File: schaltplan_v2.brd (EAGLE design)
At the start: 100 x 80 mm, 18 parts

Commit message: layout/board redesign
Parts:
- removed D10, D3, D4, D5, D6, D7, D8, D9: 1N4004, diode:DO41-10
- removed U$3, U$4, U$5: JS_05_MN_KT, n39:JS_05_MN_KT
- removed U$6, U$7, U$8: JS_05_N_K, n39:JS_05_N_K
- added T1, T2: 2N3565, transistor:TO92
- added X1: SSW-102-02-S-S-RA, con-samtec:SSW-102-02-S-S-RA
- added X3: SSW-103-02-S-S-RA, con-samtec:SSW-103-02-S-S-RA
- added X4: SSW-109-02-S-S-RA, con-samtec:SSW-109-02-S-S-RA
- U$1: value JS_05_N_K -> JS_05_MN_KT; device n39:JS_05_N_K -> n39:JS_05_MN_KT
- U$2: value JS_05_MN_KT -> JS_05_N_K; device n39:JS_05_MN_KT -> n39:JS_05_N_K
- moved D2 122.3 mm to (6.35, -40.6), turned to 0 degrees
- moved D1 91.1 mm to (6.35, -3.81), turned to 0 degrees
- moved U$2 65.0 mm to (1.27, -29.2), turned to 0 degrees
- moved U$1 58.5 mm to (1.27, -17.8), turned to 0 degrees
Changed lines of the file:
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@@
 </autorouter>
 <elements>
-<element name="D1" library="diode" package="DO41-10" value="1N4004" x="85.09" y="41.91" rot="R90"/>
-<element name="D2" library="diode" package="DO41-10" value="1N4004" x="96.52" y="41.91" rot="R90"/>
-<element name="U$1" library="n39" package="JS_05_N_K" value="JS_05_N_K" x="27.94" y="34.29" rot="R270"/>
-<element name="U$2" library="n39" package="JS_05_MN_KT" value="JS_05_MN_KT" x="15.24" y="34.29" rot="R270"/>
-<element name="U$3" library="n39" package="JS_05_MN_KT" value="JS_05_MN_KT" x="87.63" y="34.29" rot="R270"/>
-<element name="U$4" library="n39" package="JS_05_MN_KT" value="JS_05_MN_KT" x="63.5" y="34.29" rot="R270"/>
-<element name="U$5" library="n39" package="JS_05_MN_KT" value="JS_05_MN_KT" x="39.37" y="34.29" rot="R270"/>
-<element name="U$6" library="n39" package="JS_05_N_K" value="JS_05_N_K" x="3.81" y="34.29" rot="R270"/>
-<element name="U$7" library="n39" package="JS_05_N_K" value="JS_05_N_K" x="52.07" y="34.29" rot="R270"/>
-<element name="U$8" library="n39" package="JS_05_N_K" value="JS_05_N_K" x="76.2" y="34.29" rot="R270"/>
-<element name="D3" library="diode" package="DO41-10" value="1N4004" x="72.39" y="41.91" rot="R90"/>
-<element name="D4" library="diode" package="DO41-10" value="1N4004" x="60.96" y="41.91" rot="R90"/>
-<element name="D5" library="diode" package="DO41-10" value="1N4004" x="48.26" y="41.91" rot="R90"/>
-<element name="D6" library="diode" package="DO41-10" value="1N4004" x="36.83" y="41.91" rot="R90"/>
-<element name="D7" library="diode" package="DO41-10" value="1N4004" x="24.13" y="41.91" rot="R90"/>
-<element name="D8" library="diode" package="DO41-10" value="1N4004" x="12.7" y="41.91" rot="R90"/>
-<element name="D9" library="diode" package="DO41-10" value="1N4004" x="46.99" y="74.93"/>
-<element name="D10" library="diode" package="DO41-10" value="1N4004" x="59.69" y="74.93"/>
+<element name="D1" library="diode" package="DO41-10" value="1N4004" x="6.35" y="-3.81"/>
+<element name="U$1" library="n39" package="JS_05_MN_KT" value="JS_05_MN_KT" x="1.27" y="-17.78"/>
+<element name="U$2" library="n39" package="JS_05_N_K" value="JS_05_N_K" x="1.27" y="-29.21"/>
+<element name="T1" library="transistor" package="TO92" value="2N3565" x="3.81" y="-34.29"/>
+<element name="D2" library="diode" package="DO41-10" value="1N4004" x="6.35" y="-40.64"/>
+<element name="T2" library="transistor" package="TO92" value="2N3565" x="3.81" y="-46.99"/>
+<element name="X1" library="con-samtec" package="SSW-102-02-S-S-RA" value="SSW-102-02-S-S-RA" x="-5.08" y="-39.37">
+<attribute name="OC_NEWARK" value="11P9352" x="-5.08" y="-39.37" size="1.778" layer="27" display="off"/>
+<attribute name="MPN" value="SSW-102-02-S-S-RA" x="-5.08" y="-39.37" size="1.778" layer="27" display="off"/>
+<attribute name="MF" value="" x="-5.08" y="-39.37" size="1.778" layer="27" display="off"/>
+<attribute name="OC_FARNELL" value="unknown" x="-5.08" y="-39.37" size="1.778" layer="27" display="off"/>
+</element>
+<element name="X3" library="con-samtec" package="SSW-103-02-S-S-RA" value="SSW-103-02-S-S-RA" x="-3.81" y="-63.5">
+<attribute name="OC_NEWARK" value="11P9368" x="-3.81" y="-63.5" size="1.778" layer="27" display="off"/>
+<attribute name="MPN" value="SSW-103-02-S-S-RA" x="-3.81" y="-63.5" size="1.778" layer="27" display="off"/>
+<attribute name="MF" value="" x="-3.81" y="-63.5" size="1.778" layer="27" display="off"/>
+<attribute name="OC_FARNELL" value="unknown" x="-3.81" y="-63.5" size="1.778" layer="27" display="off"/>
+</element>
+<element name="X4" library="con-samtec" package="SSW-109-02-S-S-RA" value="SSW-109-02-S-S-RA" x="3.81" y="-74.93">
+<attribute name="OC_NEWARK" value="11P9466" x="3.81" y="-74.93" size="1.778" layer="27" display="off"/>
+<attribute name="MPN" value="SSW-109-02-S-S-RA" x="3.81" y="-74.93" size="1.778" layer="27" display="off"/>
+<attribute name="MF" value="" x="3.81" y="-74.93" size="1.778" layer="27" display="off"/>
+<attribute name="OC_FARNELL" value="unknown" x="3.81" y="-74.93" size="1.778" layer="27" display="off"/>
+</element>
 </elements>
 <signals>

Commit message: schaltplan_v2 finalized
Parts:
- added C1: (no value), rcl:E3,5-8
- added C2: (no value), rcl:C025-030X050
- added D10, D3, D4, D5, D6, D7, D8, D9: 1N4004, diode:DO41-10
- added R1, R2, R3, R4, R5, R6, R7, R8: (no value), resistor:0204V
- added T3, T4, T5, T6, T7, T8: 2N3565, transistor:TO92
- added U$3, U$5, U$7: JS_05_MN_KT, n39:JS_05_MN_KT
- added U$4, U$6, U$8: JS_05_N_K, n39:JS_05_N_K
- added X2: SSW-102-02-S-S-RA, con-samtec:SSW-102-02-S-S-RA
- added X5, X6, X7: SSW-103-02-S-S-RA, con-samtec:SSW-103-02-S-S-RA
- moved X4 156.2 mm to (38.1, 77.5), turned to 180 degrees
- moved X1 149.9 mm to (88.9, 77.5), turned to 180 degrees
- moved T2 118.9 mm to (74.9, 48.3)
- moved T1 115.8 mm to (85.1, 48.3)
- moved D2 108.8 mm to (78.7, 40.6), turned to 90 degrees
- moved X3 101.8 mm to (73.7, 2.54)
- moved U$1 94.4 mm to (80.0, 34.3), turned to 270 degrees
- moved D1 93.8 mm to (88.9, 40.6), turned to 90 degrees
- moved U$2 93.5 mm to (69.8, 34.3), turned to 270 degrees
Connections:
- new net N$1: X2.1, X3.1, X5.1, X6.1, X7.1
- new net N$10: C1.-, C2.2, D10.A, T1.1, T2.1, T3.1, T4.1, T5.1, T6.1, T7.1, T8.1, X4.1
- new net N$11: R2.1, X4.3
- new net N$12: D2.A, T2.3, U$2.P$1
- new net N$13: R6.2, T6.2
- new net N$14: R3.1, X4.4
- new net N$16: U$4.P$5, X5.2
- new net N$17: U$4.P$4, X5.3
- new net N$18: U$3.P$4, U$4.P$3
- new net N$2: U$2.P$5, X3.2
- new net N$20: D3.A, T3.3, U$3.P$1
- new net N$21: C1.+, C2.1, D1.C, D2.C, D3.C, D4.C, D5.C, D6.C, D7.C, D8.C, D9.C, U$1.P$2, U$2.P$2, U$3.P$2, U$4.P$2, U$5.P$2, U$6.P$2, U$7.P$2, U$8.P$2
- new net N$22: R3.2, T3.2
- new net N$23: R4.1, X4.5
- new net N$25: D4.A, T4.3, U$4.P$1
- new net N$26: R5.1, X4.6
- new net N$27: R2.2, T2.2
- new net N$28: R4.2, T4.2
- new net N$3: U$2.P$4, X3.3
- new net N$30: U$6.P$5, X6.2
- new net N$31: U$6.P$4, X6.3
- new net N$32: U$5.P$4, U$6.P$3
- new net N$34: D5.A, T5.3, U$5.P$1
- new net N$36: R5.2, T5.2
- new net N$37: R6.1, X4.7
- new net N$39: D6.A, T6.3, U$6.P$1
- new net N$4: U$1.P$4, U$2.P$3
- new net N$40: R8.2, T8.2
- new net N$42: U$8.P$5, X7.2
- new net N$43: U$8.P$4, X7.3
- new net N$44: U$7.P$4, U$8.P$3
- new net N$46: D7.A, T7.3, U$7.P$1
- new net N$48: R7.2, T7.2
- new net N$49: R7.1, X4.8
- new net N$5: U$1.P$3, U$3.P$3, U$5.P$3, U$7.P$3, X2.2
- new net N$51: D8.A, T8.3, U$8.P$1
- new net N$53: D9.A, X1.1
- new net N$54: D10.C, X1.2
- new net N$6: D1.A, T1.3, U$1.P$1
- new net N$7: R8.1, X4.9
- new net N$8: R1.2, T1.2
- new net N$9: R1.1, X4.2
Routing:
- net N$21: track 0.00 -> 262.6 mm
- net N$10: track 0.00 -> 246.6 mm
- net N$1: track 0.00 -> 110.0 mm
- net N$5: track 0.00 -> 108.6 mm
- net N$9: track 0.00 -> 59.4 mm
- net N$11: track 0.00 -> 51.8 mm
- net N$14: track 0.00 -> 42.9 mm
- net N$7: track 0.00 -> 37.8 mm
- net N$23: track 0.00 -> 35.3 mm
- net N$49: track 0.00 -> 30.2 mm
- net N$20: track 0.00 -> 28.9 mm
- net N$34: track 0.00 -> 28.8 mm
- net N$12: track 0.00 -> 28.8 mm
- net N$26: track 0.00 -> 26.4 mm
- net N$6: track 0.00 -> 23.8 mm
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
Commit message: more fixes
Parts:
- turned C1 to 270 degrees
- turned D10 to 0 degrees
- turned D9 to 180 degrees
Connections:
- removed net N$10: C1.-, C2.2, D10.A, T1.1, T2.1, T3.1, T4.1, T5.1, T6.1, T7.1, T8.1, X4.1
- removed net N$21: C1.+, C2.1, D1.C, D2.C, D3.C, D4.C, D5.C, D6.C, D7.C, D8.C, D9.C, U$1.P$2, U$2.P$2, U$3.P$2, U$4.P$2, U$5.P$2, U$6.P$2, U$7.P$2, U$8.P$2
- removed net N$53: D9.A, X1.1
- removed net N$54: D10.C, X1.2
- new net N$15: D9.C, X1.1
- new net N$19: D10.A, X1.2
- new net N$24: C1.+, C2.2, D10.C, T1.1, T2.1, T3.1, T4.1, T5.1, T6.1, T7.1, T8.1, X4.1
- new net N$29: C1.-, C2.1, D1.C, D2.C, D3.C, D4.C, D5.C, D6.C, D7.C, D8.C, D9.A, U$1.P$2, U$2.P$2, U$3.P$2, U$4.P$2, U$5.P$2, U$6.P$2, U$7.P$2, U$8.P$2
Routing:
- net N$29: track 0.00 -> 274.8 mm
- net N$21: track 262.6 -> 0.00 mm
- net N$10: track 246.6 -> 0.00 mm
- net N$24: track 0.00 -> 208.0 mm
- net N$53: track 15.0 -> 0.00 mm
- net N$15: track 0.00 -> 15.0 mm
- net N$54: track 8.64 -> 0.00 mm
- net N$19: track 0.00 -> 8.64 mm

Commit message: more fixes
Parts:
- removed X4: SSW-109-02-S-S-RA, con-samtec:SSW-109-02-S-S-RA
- added X8: SSW-110-02-S-S-RA, con-samtec:SSW-110-02-S-S-RA
- moved R1 1.27 mm to (85.1, 55.9)
- moved R2 1.27 mm to (74.9, 55.9)
- moved R3 1.27 mm to (63.5, 55.9)
- moved R4 1.27 mm to (53.3, 55.9)
- moved R5 1.27 mm to (41.9, 55.9)
- moved R6 1.27 mm to (31.8, 55.9)
- moved R7 1.27 mm to (20.3, 55.9)
- moved R8 1.27 mm to (10.2, 55.9)
- moved T1 1.27 mm to (85.1, 49.5)
- moved T2 1.27 mm to (74.9, 49.5)
- moved T3 1.27 mm to (63.5, 49.5)
- moved T4 1.27 mm to (53.3, 49.5)
- moved T5 1.27 mm to (41.9, 49.5)
- moved T6 1.27 mm to (31.8, 49.5)
- moved T7 1.27 mm to (20.3, 49.5)
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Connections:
- removed net N$29 (its old number): C1.-, C2.1, D1.C, D2.C, D3.C, D4.C, D5.C, D6.C, D7.C, D8.C, D9.A, U$1.P$2, U$2.P$2, U$3.P$2, U$4.P$2, U$5.P$2, U$6.P$2, U$7.P$2, U$8.P$2
- new net N$19: C1.-, C2.1, D9.A, T1.1, T2.1, T3.1, T4.1, T5.1, T6.1, T7.1, T8.1, X8.10
- net N$11: now also X8.3; no longer X4.3
- net N$14: now also X8.4; no longer X4.4
- net N$23: now also X8.5; no longer X4.5
- net N$24: now also D1.C, D2.C, D3.C, D4.C, D5.C, D6.C, D7.C, D8.C, U$1.P$2, U$2.P$2, U$3.P$2, U$4.P$2, U$5.P$2, U$6.P$2, U$7.P$2, U$8.P$2, X8.1; no longer T1.1, T2.1, T3.1, T4.1, T5.1, T6.1, T7.1, T8.1, X4.1
- net N$26: now also X8.6; no longer X4.6
- net N$37: now also X8.7; no longer X4.7
- net N$49: now also X8.8; no longer X4.8
- net N$7: now also X8.9; no longer X4.9
- net N$9: now also X8.2; no longer X4.2
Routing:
- net N$29 (its old number): track 274.8 -> 0.00 mm
- net N$19: track 0.00 -> 224.3 mm
- net N$24: track 208.0 -> 270.6 mm
- net N$7: track 37.8 -> 59.4 mm
- net N$49: track 30.2 -> 42.9 mm
- net N$9: track 59.4 -> 56.9 mm
- net N$11: track 51.8 -> 49.3 mm
- net N$26: track 26.4 -> 23.9 mm
- net N$23: track 35.3 -> 32.8 mm
- net N$14: track 42.9 -> 40.4 mm

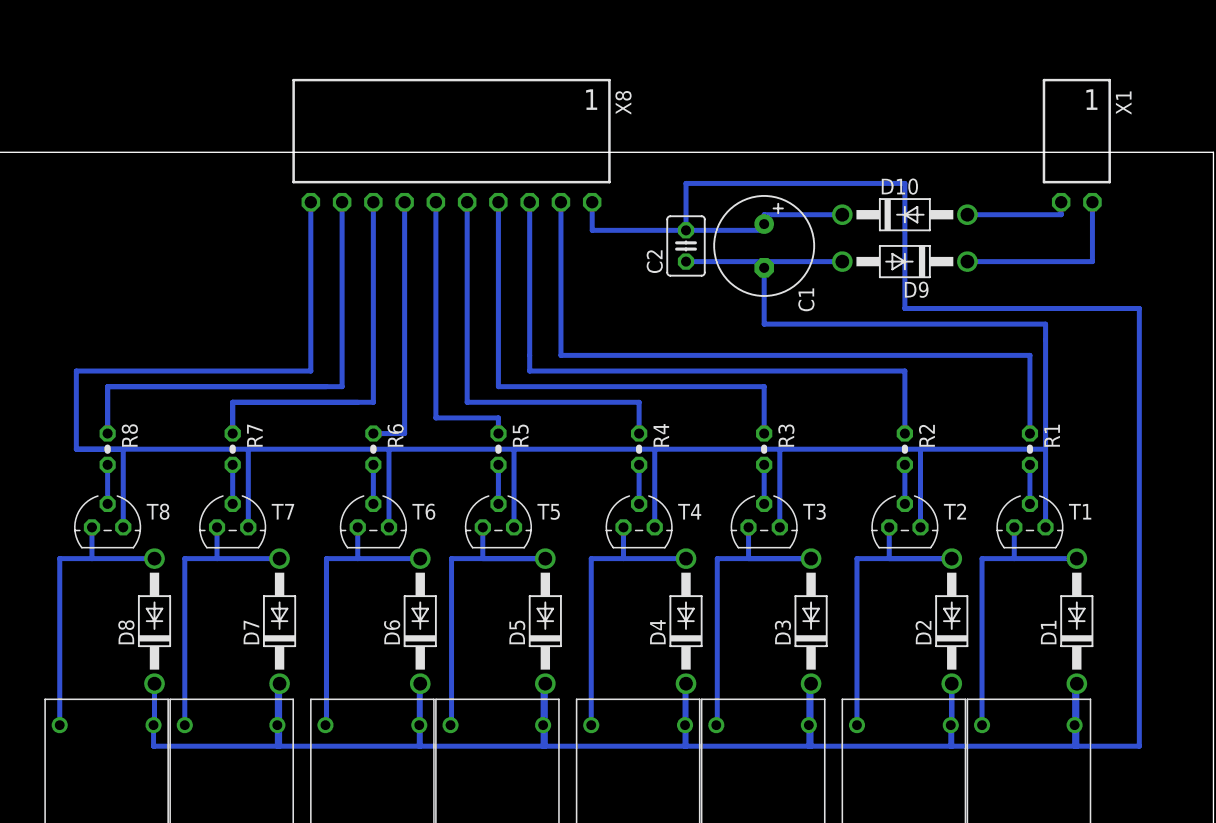
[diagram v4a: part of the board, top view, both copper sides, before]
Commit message: change 9pin connector to sub-d
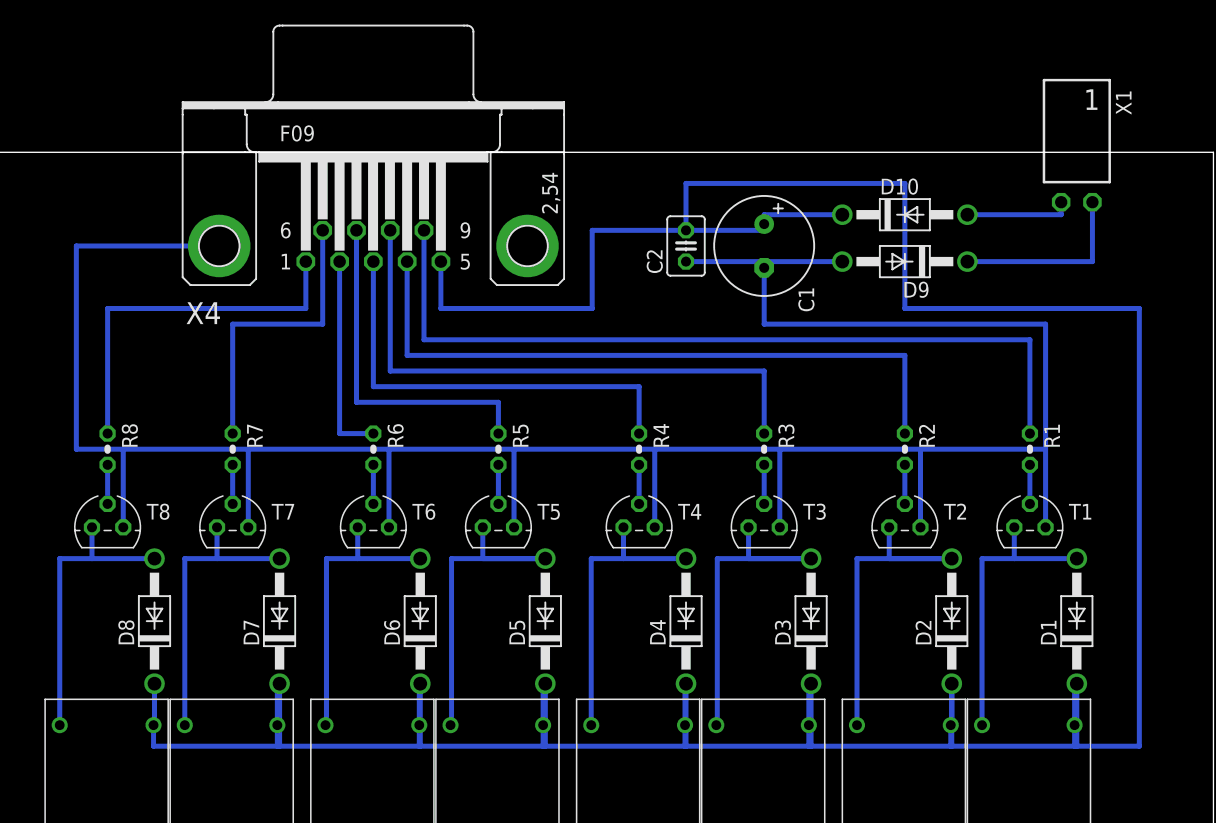
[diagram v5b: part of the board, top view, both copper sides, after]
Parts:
- removed X8: SSW-110-02-S-S-RA, con-samtec:SSW-110-02-S-S-RA
- added X4: (no value), con-subd:F09HP
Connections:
- removed net N$49: R7.1, X8.8
- removed net N$7: R8.1, X8.9
- removed net N$9: R1.1, X8.2
- new net N$15: R8.1, X4.1
- new net N$21: R7.1, X4.6
- new net N$38: R1.1, X4.9
- net N$11: now also R5.1, X4.7; no longer R2.1, X8.3
- net N$14: now also R6.1, X4.2; no longer R3.1, X8.4
- net N$19: now also X4.G1; no longer X8.10
- net N$23: now also X4.3; no longer X8.5
- net N$24: now also X4.5; no longer X8.1
- net N$26: now also R2.1, X4.4; no longer R5.1, X8.6
- net N$37: now also R3.1, X4.8; no longer R6.1, X8.7
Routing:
- net N$38: track 0.00 -> 65.7 mm
- net N$7: track 59.4 -> 0.00 mm
- net N$9: track 56.9 -> 0.00 mm
- net N$49: track 42.9 -> 0.00 mm
- net N$26: track 23.9 -> 54.4 mm
- net N$15: track 0.00 -> 30.1 mm
- net N$37: track 21.3 -> 46.9 mm
- net N$21: track 0.00 -> 23.8 mm
- net N$14: track 40.4 -> 16.7 mm
- net N$11: track 49.3 -> 28.0 mm
- net N$24: track 270.6 -> 287.7 mm
- net N$19: track 224.3 -> 208.5 mm
- net N$23: track 32.8 -> 35.6 mm

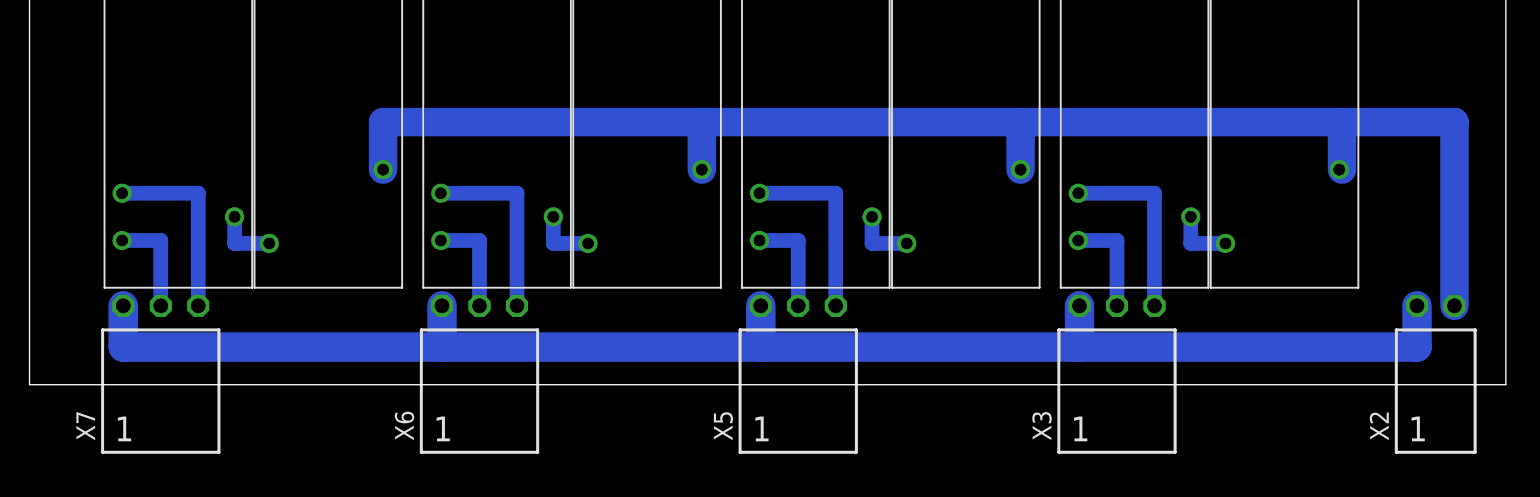
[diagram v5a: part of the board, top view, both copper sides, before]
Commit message: added correct connectors
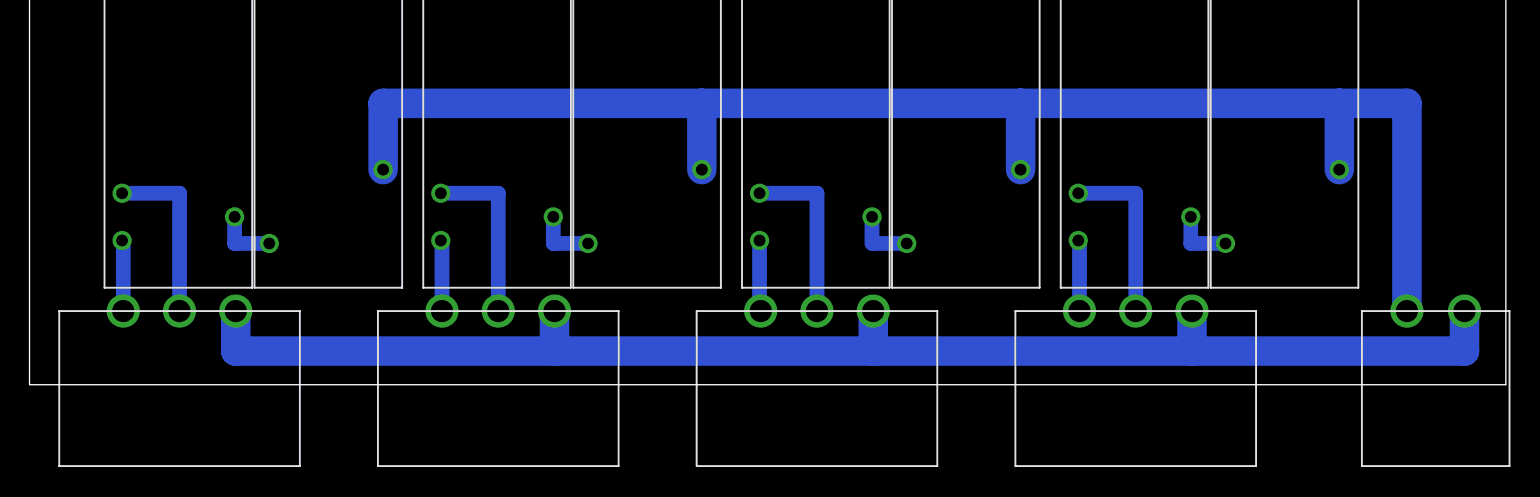
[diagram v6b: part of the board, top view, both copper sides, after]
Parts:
- removed X2: SSW-102-02-S-S-RA, con-samtec:SSW-102-02-S-S-RA
- removed X3, X5, X6, X7: SSW-103-02-S-S-RA, con-samtec:SSW-103-02-S-S-RA
- added U$10, U$11, U$12, U$13: WAGO_734_263, n39:WAGO_734_263
- added U$9: WAGO_734_262, n39:WAGO_734_262
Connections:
- net N$1: now also U$10.P$1, U$11.P$1, U$12.P$1, U$13.P$1, U$9.P$1; no longer X2.1, X3.1, X5.1, X6.1, X7.1
- net N$16: now also U$11.P$3; no longer X5.2
- net N$17: now also U$11.P$2; no longer X5.3
- net N$2: now also U$10.P$3; no longer X3.2
- net N$3: now also U$10.P$2; no longer X3.3
- net N$30: now also U$12.P$3; no longer X6.2
- net N$31: now also U$12.P$2; no longer X6.3
- net N$42: now also U$13.P$3; no longer X7.2
- net N$43: now also U$13.P$2; no longer X7.3
- net N$5: now also U$9.P$2; no longer X2.2
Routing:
- net N$1: track 110.0 -> 96.8 mm
- net N$5: track 108.6 -> 101.4 mm
- net N$42: track 7.05 -> 4.86 mm
- net N$30: track 7.05 -> 4.86 mm
- net N$16: track 7.05 -> 4.86 mm
- net N$2: track 7.05 -> 4.86 mm
- net N$31: track 12.8 -> 11.9 mm
- net N$43: track 12.8 -> 11.9 mm
- net N$3: track 12.8 -> 11.9 mm
- net N$17: track 12.8 -> 11.9 mm
